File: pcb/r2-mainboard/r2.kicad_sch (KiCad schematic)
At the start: 0 parts

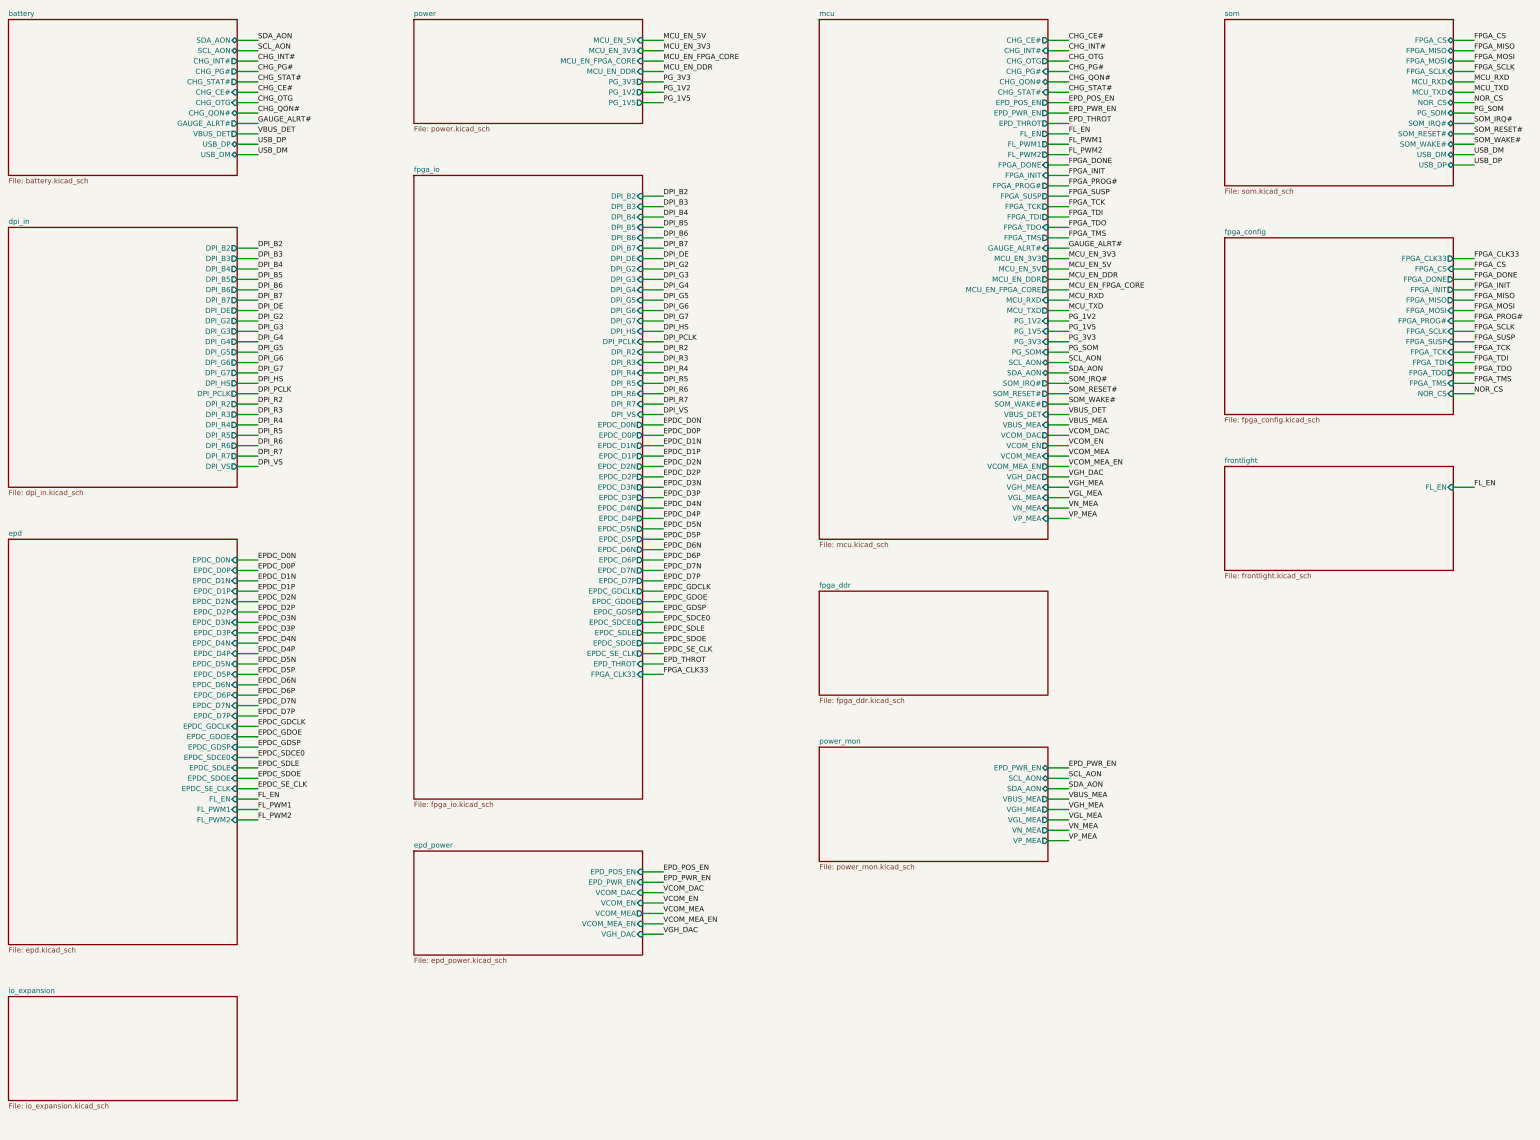
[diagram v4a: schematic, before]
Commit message: R2: WP6b -- io_expansion drawn; Stage C capture is complete
Two FPC connectors, two gated rails, seven MCU pins, everything DNP.
NOTES-R2-plan.md constraint 3 wants touch and pen "addable without a respin";
this sheet is that provision, and it is honest about which half of the promise
is certain:

  certain  -- the seven MCU pins exist and are routed, and +3V3_TOUCH /
              +3V3_PEN exist. Those are what would otherwise force a
              whole-board respin.
  a guess  -- the FPC pad order, because neither the touch controller nor the
              digitizer is chosen and the panel is not either.

docs/io-expansion.md 5 puts that in front of the owner as the last open
decision in Stage C, with three ways to close it, rather than burying it.

PC4/PC5 are USART3_TX/RX at AF0 -- verified in stm32g0b1.pdf's
alternate-function table, both free, and the one allocation here that is not
interchangeable. The other five are ordinary GPIO. Touch adds no I2C pins: it
joins the existing always-on bus, and SCL_AON/SDA_AON now carry J22.3/J22.4
alongside the charger, gauge and three INA3221s. Two spares remain, and which
two was deliberate -- PA12 (USB-DP capable) and PB12 (ADC-capable) are the two
with a capability the rest lack.

Everything DNP is coherent, not lazy: with no connector fitted there is no
load, so a fitted load switch would be two parts powering nothing. It also
means these two TPS22914s consume none of the thin LCSC stock epd-port.md 7
flags, so that stays a two-part problem.

A FOURTH SILENT SHORT, and this time the tooling caught it before the netlist
did. The connectors' GND pins dropped from their own label column and ran
straight through the two anchors below -- putting SCL_AON, SDA_AON, PEN_TXD
and PEN_RXD on GND. The entire always-on I2C bus was shorted to ground and ERC
said nothing.

So schgen.Sheet.check_label_crossings() now runs inside render() for every
generator: no wire may pass *through* a label anchor it does not end at. Ending
at an a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
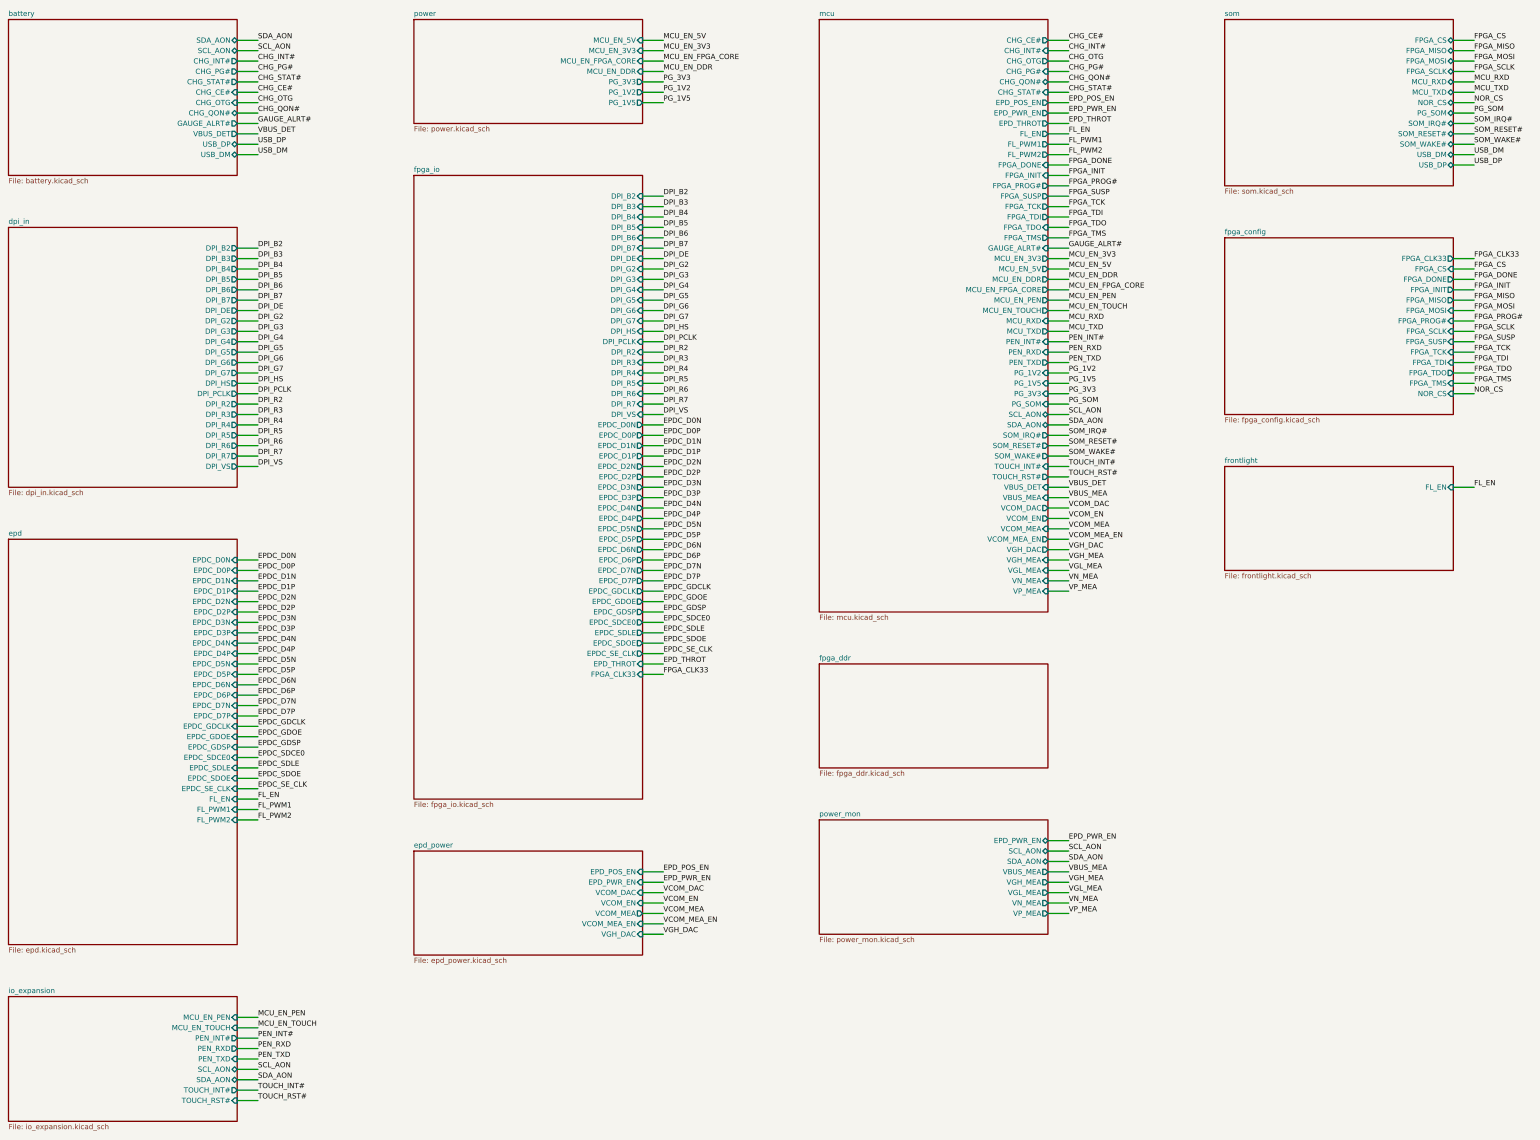
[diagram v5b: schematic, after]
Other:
- sheet io_expansion ports: added MCU_EN_PEN, MCU_EN_TOUCH, PEN_INT#, PEN_RXD, PEN_TXD, SCL_AON, SDA_AON, TOUCH_INT#, TOUCH_RST#; removed none
- sheet mcu ports: added MCU_EN_PEN, MCU_EN_TOUCH, PEN_INT#, PEN_RXD, PEN_TXD, TOUCH_INT#, TOUCH_RST#; removed none

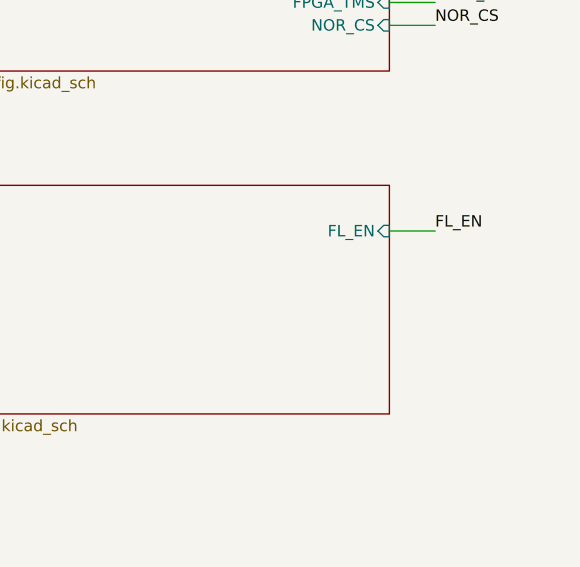
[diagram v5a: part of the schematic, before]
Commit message: R2: WP6 -- frontlight captured; it is a current driver now, not a rail
Implements docs/frontlight.md. The old sheet boosted +VSYS_FL to a 4.99 V rail
and let the panel regulate its own LED current, which is what R1 did -- R1 drove
an adapter board. GDEP103TC2-FT11's frontlight is bonded and its tail is
LED1+/LED1-/LED2+/LED2-: bare anodes and cathodes. So U53's TPS61022, its
feedback divider and the +5V2_FL net are gone, replaced by an LM3630A driving
two independently dimmed strings from +VSYS_FL, plus J24 for the tail.

Safe to regenerate rather than patch: the committed sheet's line multiset was
identical to a fresh generator run, differing only in element order, so it had
never been saved in Eeschema.

Three geometry decisions are load-bearing, not cosmetic. The symbol's pin order
was chosen twice over: SW sits beside IN because a boost wants IN -> L -> SW
adjacent, and HWEN is the lowest left pin so its 100k pull-down drops into empty
space instead of across SCL/SDA. Crossing wires are not connected in KiCad, so
that arrangement is legal and invisible -- it is the shape of the four silent
shorts of 2026-08-16, one of which shorted this same I2C bus to GND. SEL rises
to the rail in its own column for the same reason.

R509 straps SEL to IN. Grounded, the LM3630A answers at 7-bit 0x36, which is
where max17048.pdf fixes the fuel gauge; two devices on one address would take
down the always-on bus and the charger with it.

Verified: check_grid and check_label_crossings pass (they run at render time);
netlist joins FL_EN across four nodes, FL_PWM1/SCL_AON/SDA_AON across sheets,
+VSYS_FL to U53.IN, and the LED anode to C515/OVP/J24.1/J24.5; check_ucf 0
failures; ERC adds no new category. Rendered to PNG and read four times -- the
first three had text collisions that only looking would have caught, including
D34's reference printing mirrored.

schgen gains an optional prop_angle so a part placed at 180 can keep its text
upright; the default is unchanged. wire_root gain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
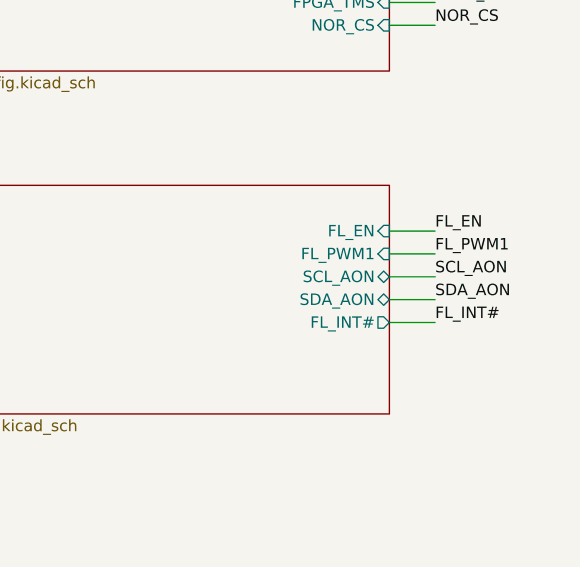
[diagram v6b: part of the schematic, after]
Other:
- sheet frontlight ports: added FL_INT#, FL_PWM1, SCL_AON, SDA_AON; removed none
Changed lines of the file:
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@@
 			)
 		)
+		(pin "FL_PWM1" input
+			(at 375.92 147.32 0)
+			(effects
+				(font
+					(size 1.27 1.27)
+				)
+				(justify right)
+			)
+		)
+		(pin "SCL_AON" bidirectional
+			(at 375.92 149.86 0)
+			(effects
+				(font
+					(size 1.27 1.27)
+				)
+				(justify right)
+			)
+		)
+		(pin "SDA_AON" bidirectional
+			(at 375.92 152.4 0)
+			(effects
+				(font
+					(size 1.27 1.27)
+				)
+				(justify right)
+			)
+		)
+		(pin "FL_INT#" output
+			(at 375.92 154.94 0)
+			(effects
+				(font
+					(size 1.27 1.27)
+				)
+				(justify right)
+			)
+		)
 		(instances
 			(project "r2"
@@
 	(wire
 		(pts
+			(xy 375.92 154.94) (xy 381.0 154.94)
+		)
+		(stroke
+			(width 0)
+			(type default)
+		)
+	)
+	(label "FL_INT#"
+		(at 381.0 154.94 0)
+		(effects
+			(font
+				(size 1.27 1.27)
+			)
+			(justify left bottom)
+		)
+	)
+	(wire
+		(pts
+			(xy 375.92 147.32) (xy 381.0 147.32)
+		)
+		(stroke
+			(width 0)
+			(type default)
+		)
+	)
+	(label "FL_PWM1"
+		(at 381.0 147.32 0)
+		(effects
+			(font
+				(size 1.27 1.27)
+			)
+			(justify left bottom)
+		)
+	)
+	(wire
+		(pts
 			(xy 78.74 223.52) (xy 83.82 223.52)
 		)
@@
 	(wire
 		(pts
+			(xy 375.92 149.86) (xy 381.0 149.86)
+		)
+		(stroke
+			(width 0)
+			(type default)
+		)
+	)
+	(label "SCL_AON"
+		(at 381.0 149.86 0)
+		(effects
+			(font
+				(size 1.27 1.27)
+			)
+			(justify left bottom)
+		)
+	)
+	(wire
+		(pts
 			(xy 78.74 38.1) (xy 83.82 38.1)
 		)
@@
 		(effects
 			(font
+				(size 1.27 1.27)
+			)
+			(justify left bottom)
+		)
+	)
+	(wire
+		(pts
+			(xy 375.92 152.4) (xy 381.0 152.4)
+		)
+		(stroke
+			(width 0)
+			(type default)
+		)
+	)
+	(label "SDA_AON"
+		(at 381.0 152.4 0)
+		(effects
+			(font
